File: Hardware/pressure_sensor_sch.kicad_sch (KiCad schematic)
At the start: 83 parts, among them J10 1053131104, J11 1053131104, J13 1053131104, J6 1053131104, J8 1053131104, J9 1053131104, U7 ADS131M06IPBS

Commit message: updated sensors and other stuff
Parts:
- removed J11, J13: 1053131104, Connector_Molex:Molex_Nano-Fit_105313-xx04_1x04_P2.50mm_Horizontal, symbol iclr:1053131104
- removed JP30, JP35, JP39 (x2): SolderJumper_3_Open, Jumper:SolderJumper-3_P1.3mm_Open_RoundedPad1.0x1.5mm_NumberLabels, symbol Jumper:SolderJumper_3_Open
- added J4, J7: 1053131104, Connector_Molex:Molex_Pico-Clasp_202396-0407_1x04-1MP_P1.00mm_Horizontal, symbol iclr:1053131104
- added JP10, JP20, JP3, JP5: SolderJumper_3_Open, iclr:small_3pin_SolderJP, symbol Jumper:SolderJumper_3_Open
- J10, J6, J8, J9: footprint Connector_Molex:Molex_Nano-Fit_105313-xx04_1x04_P2.50mm_Horizontal -> Connector_Molex:Molex_Pico-Clasp_202396-0407_1x04-1MP_P1.00mm_Horizontal
- JP12, JP13, JP14, JP17, JP18, JP19, JP23, JP24, JP25, JP28, JP29, JP33, JP6, JP7: footprint Jumper:SolderJumper-3_P1.3mm_Open_RoundedPad1.0x1.5mm_NumberLabels -> iclr:small_3pin_SolderJP
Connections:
- net +12V: now also JP10.3 (B)
- net +5V: now also JP10.1 (A)
- net AIN0N: now also C38.2, R40.1; no longer C38.1, R39.1
- net AIN0P: now also C38.1, R39.1; no longer C38.2, R40.1
- net AIN1N: now also C33.2, R47.1; no longer C33.1, R46.1
- net AIN1P: now also C33.1, R46.1; no longer C33.2, R47.1
- net AIN2N: now also C42.2, R58.1; no longer C42.1, R57.1
- net AIN2P: now also C42.1, R57.1; no longer C42.2, R58.1
- net AIN3N: now also C41.2, R52.1; no longer C41.1, R51.1
- net AIN3P: now also C41.1, R51.1; no longer C41.2, R52.1
- net AIN4N: now also C44.2, R103.1; no longer C44.1, R102.1
- net AIN4P: now also C44.1, R102.1; no longer C44.2, R103.1
- net AIN5N: now also C43.2, R97.1; no longer C43.1, R96.1
- net AIN5P: now also C43.1, R96.1; no longer C43.2, R97.1
- net GND: now also J10.1, J6.1, J8.1, J9.1, J4.1, J7.1; no longer C39.2, J10.4, J6.4, J8.4, J9.4, U7.13 (AGND), U7.28 (AGND)
- net at JP31.2 (B), R47.2, R49.1: now also J7.2
- net at JP33.2 (C): now also J9.4
- net at JP25.2 (C): now also J9.3
- net at JP27.2 (B), R97.2, R98.1: now also J9.2
- net at JP16.2 (B), R52.2, R53.1: now also J6.2; no longer J9.3
- net at JP12.2 (C): now also J4.4; no longer J6.1
- net at R61.1, R61.2: now also JP20.1 (A)
- net at JP11.2 (B), R40.2, R41.1: now also J4.2; no longer J6.3
- net at JP32.2 (B), R103.2, R104.1: now also J10.2; no longer J10.3
- net at JP4.2 (B), R46.2: now also JP20.2 (C), JP5.1 (A)
- net at R61.1: now also JP5.3 (B)
- net at JP23.2 (C): now also J6.4; no longer J9.1
- net at R61.1, R61.2: now also JP20.3 (B)
- net at JP28.2 (C): now also J10.4; no longer J10.1
- net at R99.1: now also JP29.3 (B)
- net at R100.1, R99.2: now also JP3.3 (B); no longer JP29.3 (B)
- net at R100.2, R101.1: now also JP3.1 (A); no longer JP29.1 (A)
- net at JP22.2 (B), R58.2, R59.1: now also J8.2; no longer J8.3
- net at JP17.2 (C): now also J8.4; no longer J8.1
- net at JP7.2 (C): now also J4.3; no longer J6.2
- net at JP31.2 (B), R102.2: now also JP29.1 (A), JP3.2 (C); no longer JP29.2 (C)
- net at JP14.2 (C): now also J6.3; no longer J9.2
- net at JP19.2 (C): now also J8.3; no longer J8.2
- new net: J7.4, JP10.2 (C)
- new net: J7.3, JP5.2 (C)
- new net: J10.3, JP29.2 (C)
- new net GNDA: C39.2, U7.13 (AGND), U7.28 (AGND)
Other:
- note added: "Voltage option"
- note removed: "Volatge option"
- note removed: "Voltage drawn across R34, R39, and R44 to be 1.2v max to match ADS input range"

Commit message: rearranged comps
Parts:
- added C79, C85: 0.01uF, Capacitor_SMD:C_0402_1005Metric, symbol Device:C_Small
- added C80, C86, C87: 0.1uF, Capacitor_SMD:C_0402_1005Metric, symbol Device:C_Small
- added R111, R112: 100, Resistor_SMD:R_0402_1005Metric, symbol Device:R_Small
- added TC1: Thermocouple, Connector_Molex:Molex_Nano-Fit_105313-xx02_1x02_P2.50mm_Horizontal, symbol Device:Thermocouple
- added U13: MAX31856, Package_SO:TSSOP-14_4.4x5mm_P0.65mm, symbol Sensor_Temperature:MAX31856
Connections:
- net +3.3V: now also C86.2, C87.2, U13.5 (AVDD), U13.8 (DVDD)
- net GND: now also C79.1, C85.2, C86.1, C87.1, U13.1 (AGND), U13.14 (DGND)
- net ADS_MISO renamed MISO
- net MISO: now also U13.11 (SDO)
- net ADS_MOSI renamed MOSI
- net MOSI: now also U13.12 (SDI)
- net ADS_SCLK renamed SCLK
- net SCLK: now also U13.10 (SCK)
- net DRDY renamed ADS_DRDY
- new net: C79.2, C80.1, R111.1, U13.4 (T+)
- new net: C80.2, C85.1, R112.2, U13.3 (T-)
- new net: R112.1, TC1.2 (-), U13.2 (BIAS)
- new net: R111.2, TC1.1 (+)
- new net TC_CS: U13.9 (~{CS})
- new net TC_DRDY: U13.7 (~{DRDY})
- new net TC_FAULT: U13.13 (~{FAULT})
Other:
- moved on the sheet: C39, C41, C43, C46, U7

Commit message: Finished Boosts and Sensors
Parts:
- added C88: 0.1uF, Capacitor_SMD:C_0402_1005Metric, symbol Device:C_Small
- renumbered C39 to C37, C43 to C81, C46 to C82, C41 to C84, JP31 to JP8, R61 to R74, R61 to R75, R61 to R76
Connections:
- net +3.3V: now also C88.2
- net GNDA: now also C88.1

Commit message: v2 Ready for Review
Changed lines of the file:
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@@
 		)
 		(property "Value" "GNDA"
-			(at 104.648 41.656 0)
+			(at 105.46 39.31 0)
 			(effects
 				(font

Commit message: Most Review Changes
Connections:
- net GND: no longer J10.1, J4.1, J6.1, J7.1, J8.1, J9.1, JP11.1 (A), JP16.1 (A), JP22.1 (A), JP27.1 (A), JP32.1 (A), JP8.1 (A), R101.2, R38.2, R50.2, R56.2, R76.2, R95.2
- net GNDA: now also J10.1, J4.1, J6.1, J7.1, J8.1, J9.1, JP11.1 (A), JP16.1 (A), JP22.1 (A), JP27.1 (A), JP32.1 (A), JP8.1 (A), R101.2, R38.2, R50.2, R56.2, R76.2, R95.2

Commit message: Replaced PicoClasp with nanofits
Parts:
- removed J4: 1053131104, Connector_Molex:Molex_Pico-Clasp_202396-0407_1x04-1MP_P1.00mm_Horizontal, symbol iclr:1053131104
- added J13: 1053131104, Connector_Molex:Molex_Nano-Fit_105313-xx04_1x04_P2.50mm_Horizontal, symbol iclr:1053131104
- J10, J6, J7, J8, J9: footprint Connector_Molex:Molex_Pico-Clasp_202396-0407_1x04-1MP_P1.00mm_Horizontal -> Connector_Molex:Molex_Nano-Fit_105313-xx04_1x04_P2.50mm_Horizontal
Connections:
- net GNDA: now also J10.4, J6.4, J7.4, J8.4, J9.4, J13.4; no longer J10.1, J6.1, J7.1, J8.1, J9.1
- net at JP16.2 (B), R52.2, R53.1: now also J8.3; no longer J6.2
- net at JP11.2 (B), R40.2, R41.1: now also J7.3
- net at JP10.2 (C): now also J6.1; no longer J7.4
- net at JP32.2 (B), R103.2, R104.1: now also J13.3; no longer J10.2
- net at JP5.2 (C): now also J6.2; no longer J7.3
- net at JP8.2 (B), R47.2, R49.1: now also J6.3; no longer J7.2
- net at JP22.2 (B), R58.2, R59.1: now also J9.3; no longer J8.2
- net at JP25.2 (C): now also J10.2; no longer J9.3
- net at JP27.2 (B), R97.2, R98.1: now also J10.3; no longer J9.2
- net at JP14.2 (C): now also J8.2; no longer J6.3
- net at JP23.2 (C): now also J8.1; no longer J6.4
- net at JP29.2 (C): now also J13.2; no longer J10.3
- net at JP28.2 (C): now also J13.1; no longer J10.4
- net at JP12.2 (C): now also J7.1
- net at JP19.2 (C): now also J9.2; no longer J8.3
- net at JP33.2 (C): now also J10.1; no longer J9.4
- net at JP7.2 (C): now also J7.2
- net at JP17.2 (C): now also J9.1; no longer J8.4

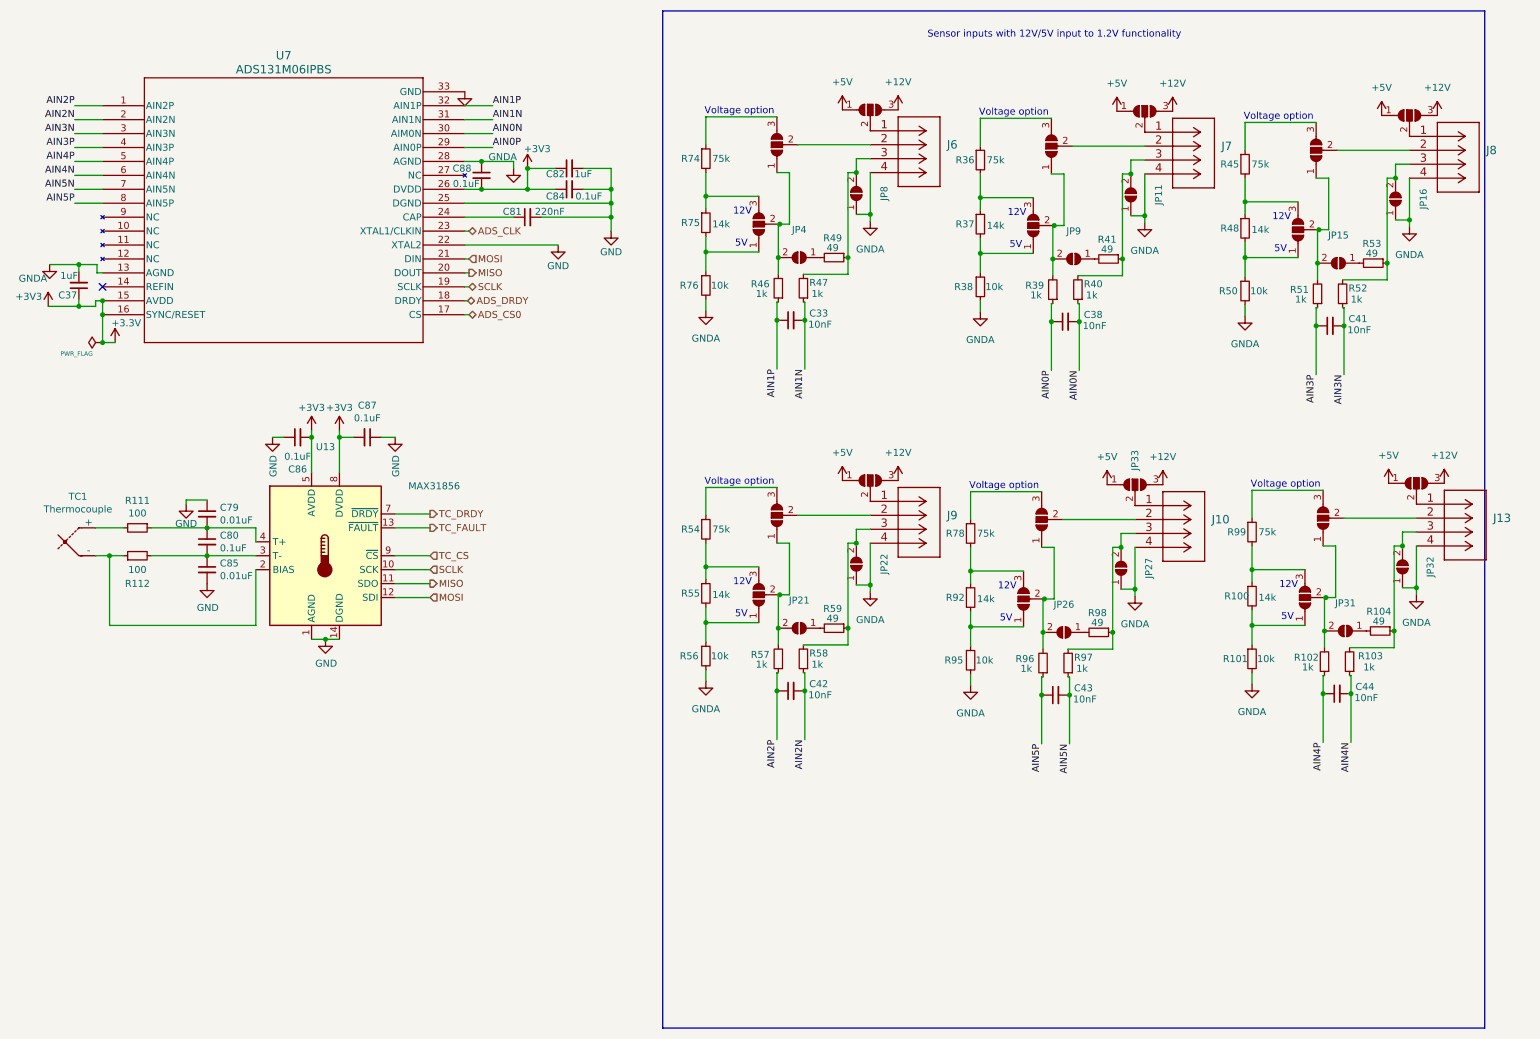
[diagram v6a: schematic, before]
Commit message: schematic reformatting and bom consolidation
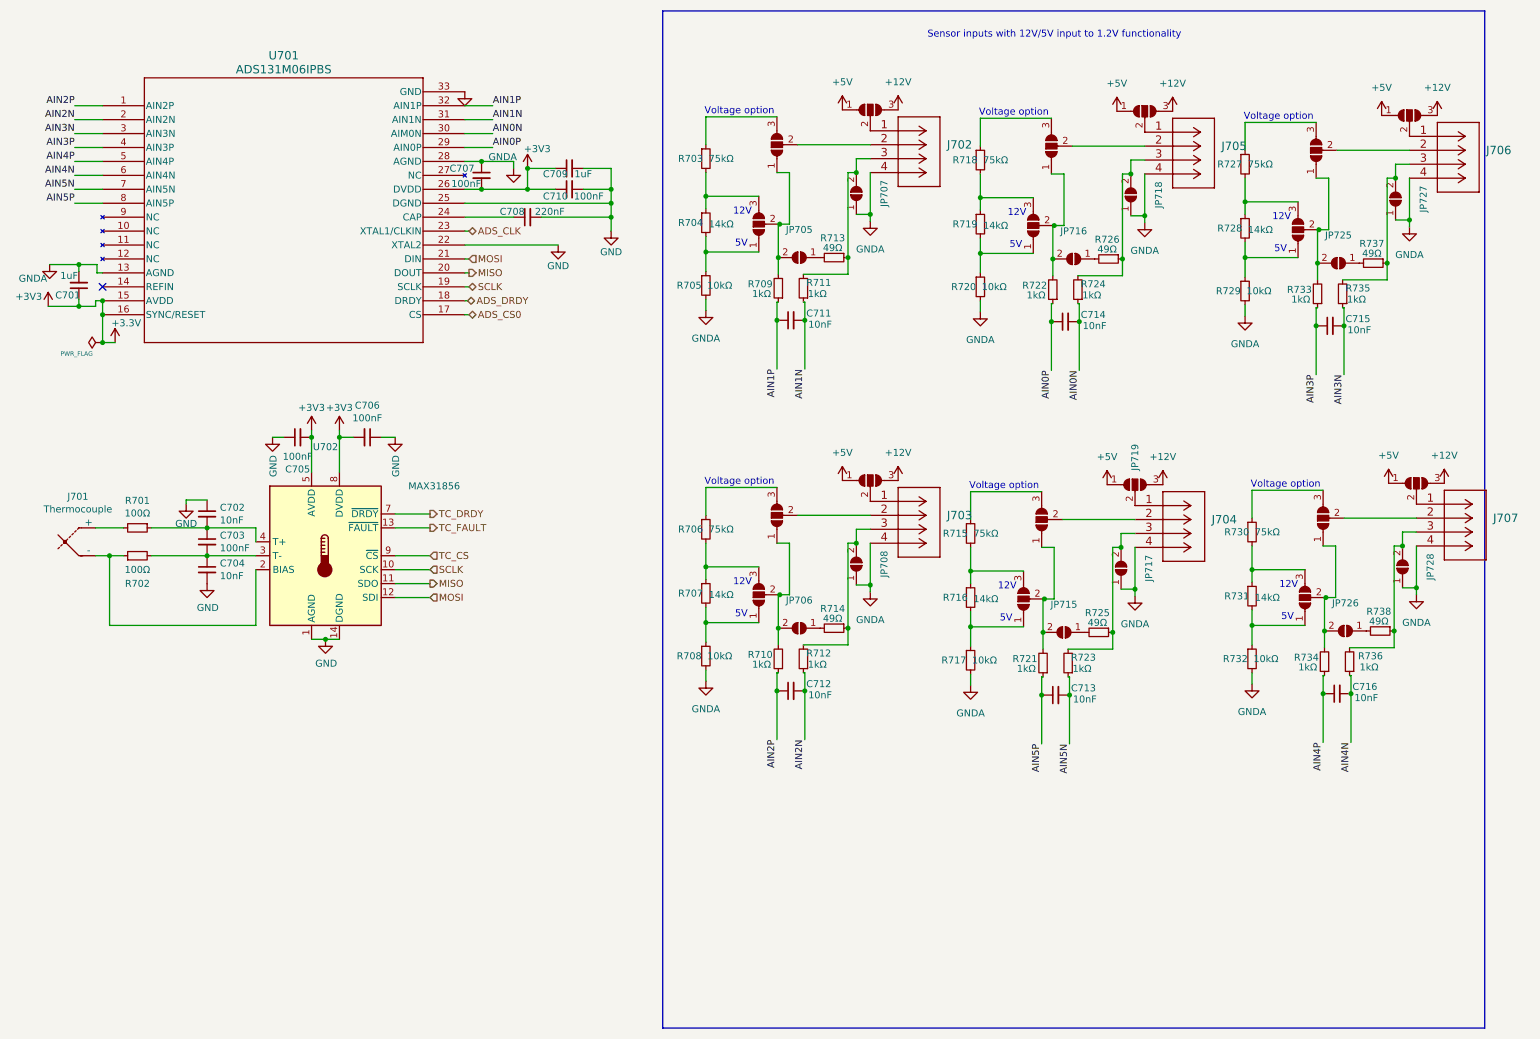
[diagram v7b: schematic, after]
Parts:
- C702: renamed from C79; value 0.01uF -> 10nF
- C703: renamed from C80; value 0.1uF -> 100nF
- C704: renamed from C85; value 0.01uF -> 10nF
- C705: renamed from C86; value 0.1uF -> 100nF
- C706: renamed from C87; value 0.1uF -> 100nF
- C707: renamed from C88; value 0.1uF -> 100nF
- C710: renamed from C84; value 0.1uF -> 100nF
- JP701: renamed from JP20; now left out of the parts list
- JP702: renamed from JP18; now left out of the parts list
- JP703: renamed from JP5; now left out of the parts list
- JP704: renamed from JP19; now left out of the parts list
- JP705: renamed from JP4; now left out of the parts list
- JP706: renamed from JP21; now left out of the parts list
- JP707: renamed from JP8; now left out of the parts list
- JP708: renamed from JP22; now left out of the parts list
- JP709: renamed from JP10; now left out of the parts list
- JP710: renamed from JP17; now left out of the parts list
- JP711: renamed from JP24; now left out of the parts list
- JP712: renamed from JP6; now left out of the parts list
- JP713: renamed from JP25; now left out of the parts list
- JP714: renamed from JP7; now left out of the parts list
- JP715: renamed from JP26; now left out of the parts list
- JP716: renamed from JP9; now left out of the parts list
- JP717: renamed from JP27; now left out of the parts list
- JP718: renamed from JP11; now left out of the parts list
- JP719: renamed from JP33; now left out of the parts list
- JP720: renamed from JP12; now left out of the parts list
- JP721: renamed from JP13; now left out of the parts list
- JP722: renamed from JP3; now left out of the parts list
- JP723: renamed from JP14; now left out of the parts list
- JP724: renamed from JP29; now left out of the parts list
- JP725: renamed from JP15; now left out of the parts list
- JP726: renamed from JP31; now left out of the parts list
- JP727: renamed from JP16; now left out of the parts list
- JP728: renamed from JP32; now left out of the parts list
- JP729: renamed from JP23; now left out of the parts list
- JP730: renamed from JP28; now left out of the parts list
- R701: renamed from R111; value 100 -> 100Ω
- R702: renamed from R112; value 100 -> 100Ω
- R703: renamed from R74; value 75k -> 75kΩ
- R704: renamed from R75; value 14k -> 14kΩ
- R705: renamed from R76; value 10k -> 10kΩ
- R706: renamed from R54; value 75k -> 75kΩ
- R707: renamed from R55; value 14k -> 14kΩ
- R708: renamed from R56; value 10k -> 10kΩ
- R709: renamed from R46; value 1k -> 1kΩ
- R710: renamed from R57; value 1k -> 1kΩ
- R711: renamed from R47; value 1k -> 1kΩ
- R712: renamed from R58; value 1k -> 1kΩ
- R713: renamed from R49; value 49 -> 49Ω
- R714: renamed from R59; value 49 -> 49Ω
- R715: renamed from R78; value 75k -> 75kΩ
- R716: renamed from R92; value 14k -> 14kΩ
- R717: renamed from R95; value 10k -> 10kΩ
- R718: renamed from R36; value 75k -> 75kΩ
- R719: renamed from R37; value 14k -> 14kΩ
- R720: renamed from R38; value 10k -> 10kΩ
- R721: renamed from R96; value 1k -> 1kΩ
- R722: renamed from R39; value 1k -> 1kΩ
- R723: renamed from R97; value 1k -> 1kΩ
- R724: renamed from R40; value 1k -> 1kΩ
- R725: renamed from R98; value 49 -> 49Ω
- R726: renamed from R41; value 49 -> 49Ω
- R727: renamed from R45; value 75k -> 75kΩ
- R728: renamed from R48; value 14k -> 14kΩ
- R729: renamed from R50; value 10k -> 10kΩ
- R730: renamed from R99; value 75k -> 75kΩ
- R731: renamed from R100; value 14k -> 14kΩ
- R732: renamed from R101; value 10k -> 10kΩ
- R733: renamed from R51; value 1k -> 1kΩ
- R734: renamed from R102; value 1k -> 1kΩ
- R735: renamed from R52; value 1k -> 1kΩ
- R736: renamed from R103; value 1k -> 1kΩ
- R737: renamed from R53; value 49 -> 49Ω
- R738: renamed from R104; value 49 -> 49Ω
- renumbered C37 to C701, C81 to C708, C82 to C709, C33 to C711, C42 to C712, C43 to C713, C38 to C714, C41 to C715, C44 to C716, TC1 to J701, J6 to J702, J9 to J703, J10 to J704, J7 to J705, J8 to J706, J13 to J707, U7 to U701, U13 to U702
